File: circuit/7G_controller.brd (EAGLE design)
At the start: 66.3 x 72 mm, 18 parts, among them Q1 3.6864MHz

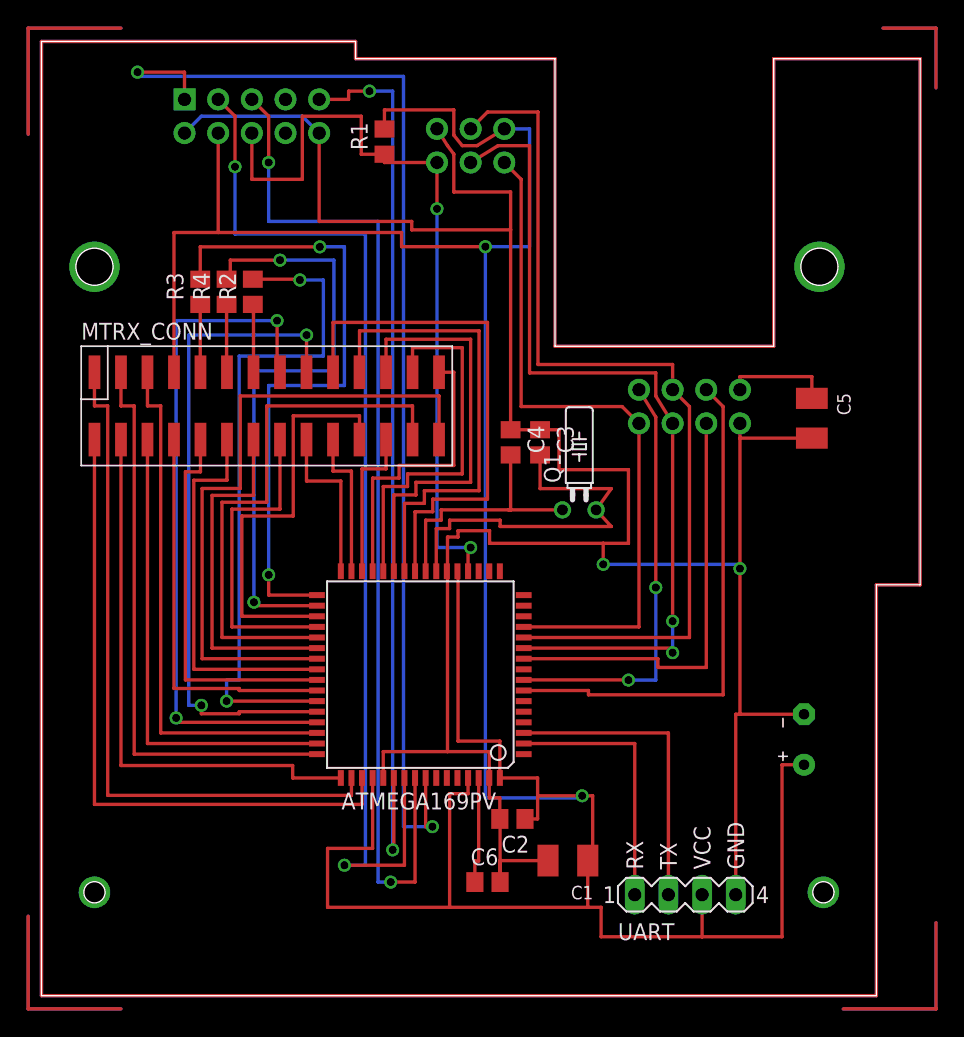
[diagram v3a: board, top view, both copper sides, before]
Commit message: 
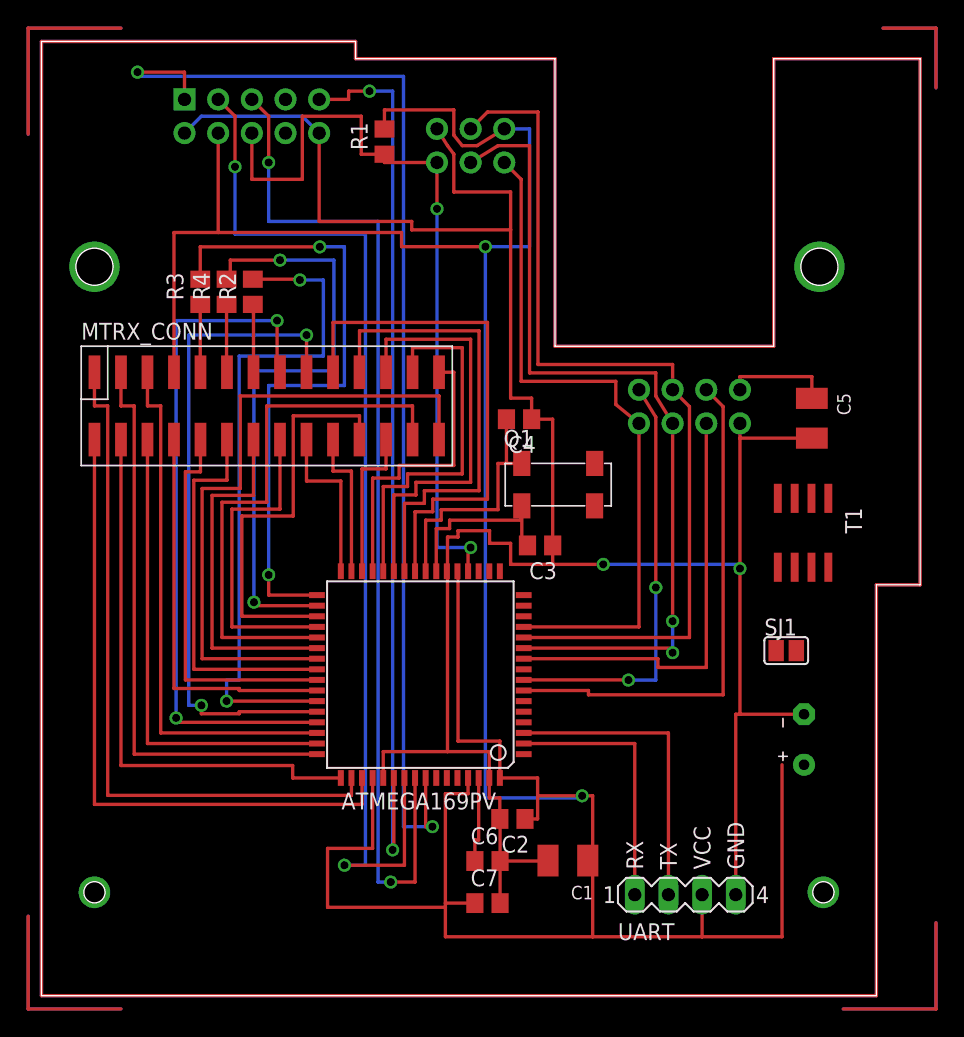
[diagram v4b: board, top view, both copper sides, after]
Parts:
- added C7: 100nF, rcl:C0805
- added SJ1: (no value), jumper:SJ
- added T1: TPS1101D, KileParts:SO8
- C5: value 1uF -> 4.7uF
- NRF24L01: value NRF24L01_MOD_NINE_EAGLES -> NRF24L01_MOD_NINE_EAGLESGENERIC
- Q1: value 3.6864MHz -> 32768Hz; device crystal:TC26H -> KileParts:NSK_QUARTZ_CLOCK
- moved C3 7.78 mm to (37.6, 34.0), turned to 180 degrees
- moved Q1 2.48 mm to (39.0, 38.6)
- moved C4 1.86 mm to (36.0, 43.5), turned to 180 degrees
- moved C6 1.59 mm to (33.7, 10.2)
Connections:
- removed net N$7: ATMEGA169PV.23, C3.2, Q1.2
- new net N$4: BAT1.+, SJ1.2, T1.5, T1.6, T1.7, T1.8
- new net N$6: ATMEGA169PV.23, C3.2, Q1.1
- net GND: now also C7.2, T1.4
- net N$8: now also Q1.4; no longer Q1.1
- net VCC: now also C7.1, SJ1.1, T1.1, T1.2, T1.3; no longer BAT1.+
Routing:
- net N$7: track 29.1 -> 0.00 mm
- net N$6: track 0.00 -> 14.8 mm
- net GND: track 193.4 -> 187.3 mm
- net VCC: track 244.3 -> 247.9 mm
- net AREF: track 8.14 -> 6.55 mm

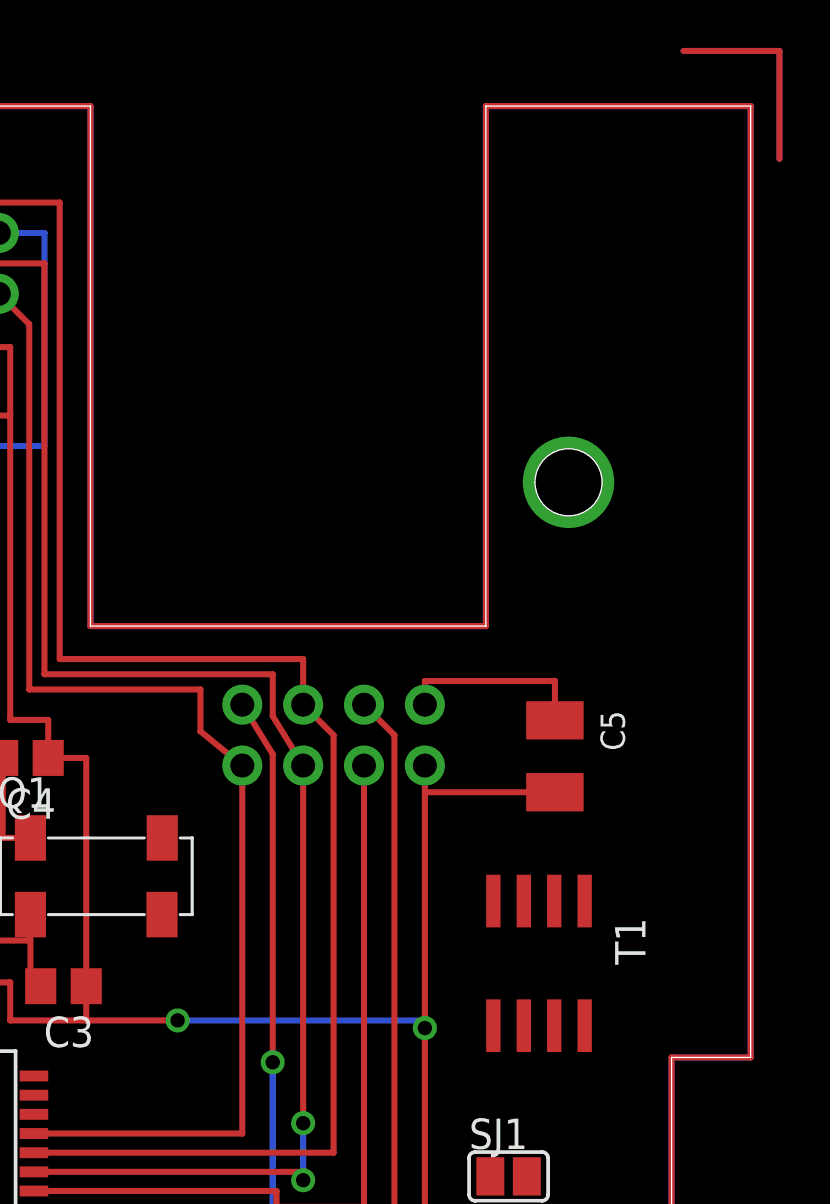
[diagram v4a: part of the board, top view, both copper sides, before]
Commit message: 
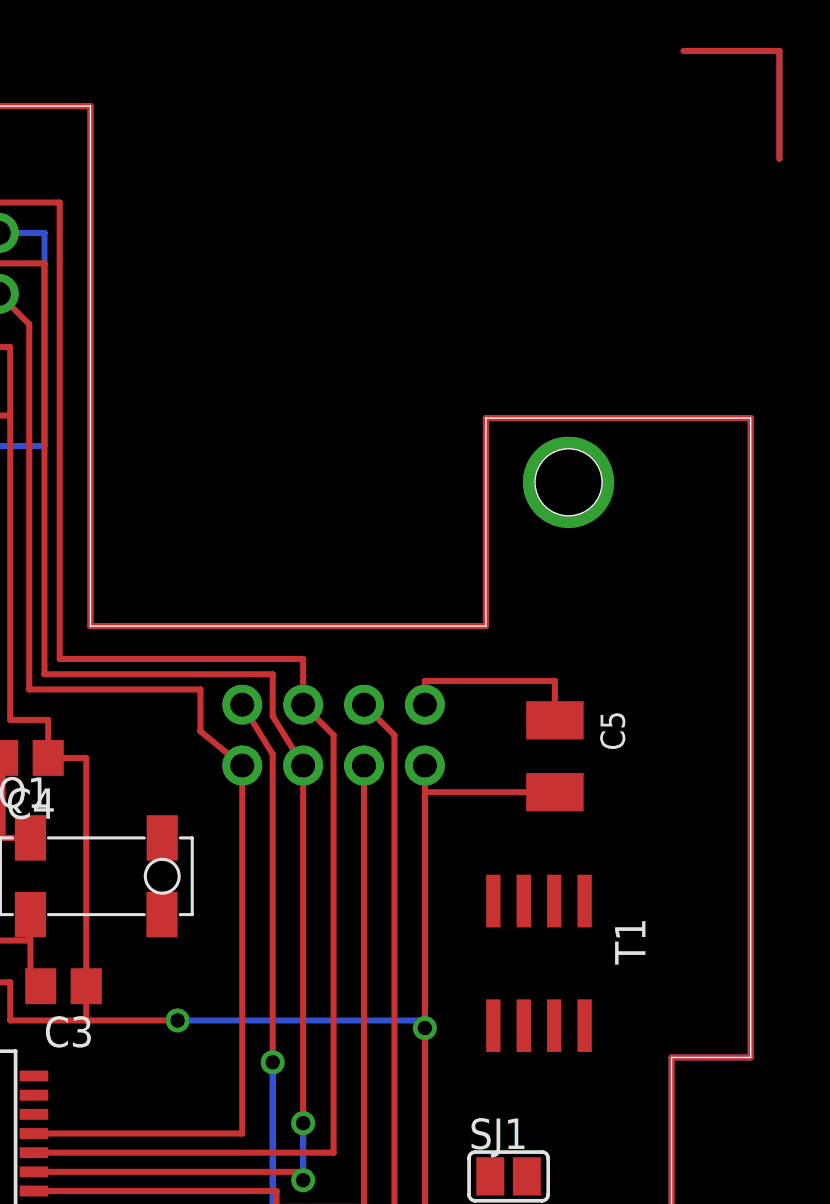
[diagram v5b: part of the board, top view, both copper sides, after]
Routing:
- net N$19: track 320.0 -> 294.0 mm
- net N$1: track 320.0 -> 294.0 mm
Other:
- outline, holes or cut-outs redrawn
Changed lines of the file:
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@@
 <setting verticaltext="up"/>
 </settings>
-<grid distance="0.00625" unitdist="inch" unit="inch" style="lines" multiple="1" display="yes" altdistance="0.025" altunitdist="inch" altunit="inch"/>
+<grid distance="0.0125" unitdist="inch" unit="inch" style="lines" multiple="1" display="yes" altdistance="0.025" altunitdist="inch" altunit="inch"/>
 <layers>
 <layer number="1" name="Top" color="4" fill="1" visible="yes" active="yes"/>
@@
 <wire x1="63" y1="0" x2="63" y2="31" width="0" layer="20"/>
 <wire x1="63" y1="31" x2="66.3" y2="31" width="0" layer="20"/>
-<wire x1="66.3" y1="31" x2="66.3" y2="70.7" width="0" layer="20"/>
-<wire x1="66.3" y1="70.7" x2="55.25" y2="70.7" width="0" layer="20"/>
-<wire x1="55.25" y1="70.7" x2="55.25" y2="49" width="0" layer="20"/>
+<wire x1="66.3" y1="31" x2="66.3" y2="57.6825" width="0" layer="20"/>
+<wire x1="66.3" y1="57.6825" x2="55.25" y2="57.6825" width="0" layer="20"/>
+<wire x1="55.25" y1="57.6825" x2="55.25" y2="49" width="0" layer="20"/>
 <wire x1="55.25" y1="49" x2="38.75" y2="49" width="0" layer="20"/>
 <wire x1="38.75" y1="49" x2="38.75" y2="70.7" width="0" layer="20"/>
@@
 <wire x1="38.75" y1="70.7" x2="38.75" y2="49" width="0.254" layer="16"/>
 <wire x1="38.75" y1="49" x2="55.25" y2="49" width="0.254" layer="16"/>
-<wire x1="55.25" y1="49" x2="55.25" y2="70.7" width="0.254" layer="16"/>
-<wire x1="55.25" y1="70.7" x2="66.3" y2="70.7" width="0.254" layer="16"/>
-<wire x1="66.3" y1="70.7" x2="66.3" y2="31" width="0.254" layer="16"/>
+<wire x1="55.25" y1="49" x2="55.25" y2="57.6825" width="0.254" layer="16"/>
+<wire x1="55.25" y1="57.6825" x2="66.3" y2="57.6825" width="0.254" layer="16"/>
+<wire x1="66.3" y1="57.6825" x2="66.3" y2="31" width="0.254" layer="16"/>
 <wire x1="66.3" y1="31" x2="63" y2="31" width="0.254" layer="16"/>
 <wire x1="63" y1="31" x2="63" y2="0" width="0.254" layer="16"/>
@@
 <wire x1="38.75" y1="70.7" x2="38.75" y2="49" width="0.254" layer="1"/>
 <wire x1="38.75" y1="49" x2="55.25" y2="49" width="0.254" layer="1"/>
-<wire x1="55.25" y1="49" x2="55.25" y2="70.7" width="0.254" layer="1"/>
-<wire x1="55.25" y1="70.7" x2="66.3" y2="70.7" width="0.254" layer="1"/>
-<wire x1="66.3" y1="70.7" x2="66.3" y2="31" width="0.254" layer="1"/>
+<wire x1="55.25" y1="49" x2="55.25" y2="57.6825" width="0.254" layer="1"/>
+<wire x1="55.25" y1="57.6825" x2="66.3" y2="57.6825" width="0.254" layer="1"/>
+<wire x1="66.3" y1="57.6825" x2="66.3" y2="31" width="0.254" layer="1"/>
 <wire x1="66.3" y1="31" x2="63" y2="31" width="0.254" layer="1"/>
 <wire x1="63" y1="31" x2="63" y2="0" width="0.254" layer="1"/>

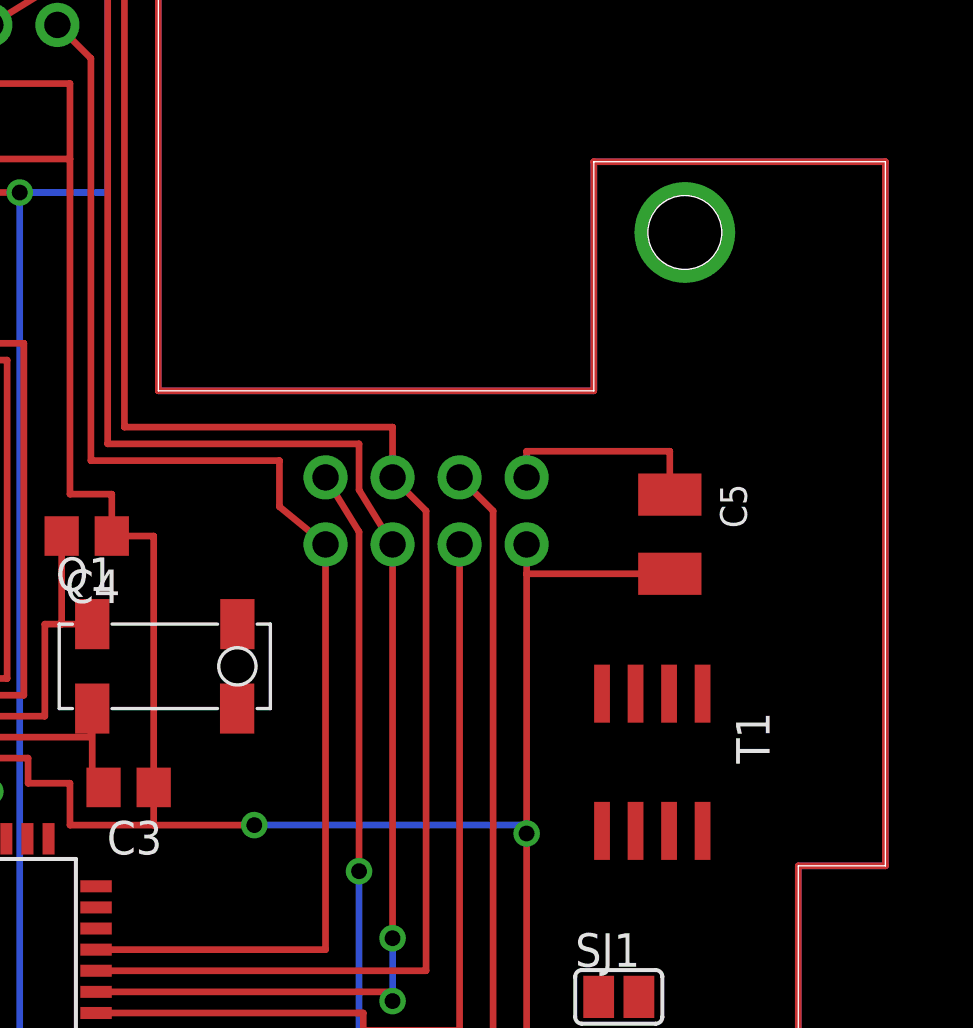
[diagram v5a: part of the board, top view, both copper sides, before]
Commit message: 
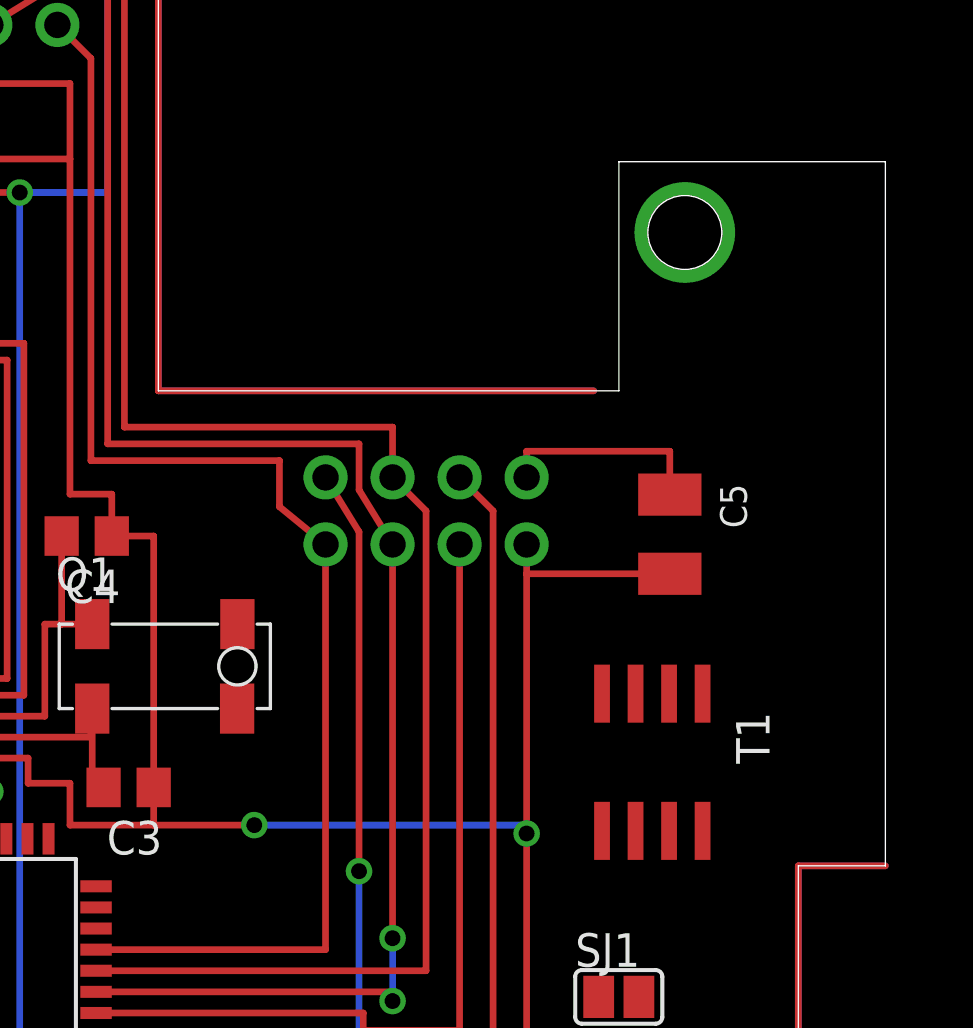
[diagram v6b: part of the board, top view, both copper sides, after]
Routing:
- net N$19: track 294.0 -> 247.6 mm
- net N$1: track 294.0 -> 247.6 mm
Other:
- outline, holes or cut-outs redrawn
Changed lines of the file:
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@@
 <wire x1="63" y1="31" x2="66.3" y2="31" width="0" layer="20"/>
 <wire x1="66.3" y1="31" x2="66.3" y2="57.6825" width="0" layer="20"/>
-<wire x1="66.3" y1="57.6825" x2="55.25" y2="57.6825" width="0" layer="20"/>
-<wire x1="55.25" y1="57.6825" x2="55.25" y2="49" width="0" layer="20"/>
-<wire x1="55.25" y1="49" x2="38.75" y2="49" width="0" layer="20"/>
+<wire x1="66.3" y1="57.6825" x2="56.2025" y2="57.6825" width="0" layer="20"/>
+<wire x1="56.2025" y1="57.6825" x2="56.2025" y2="49" width="0" layer="20"/>
+<wire x1="56.2025" y1="49" x2="38.75" y2="49" width="0" layer="20"/>
 <wire x1="38.75" y1="49" x2="38.75" y2="70.7" width="0" layer="20"/>
 <wire x1="38.75" y1="70.7" x2="23.7" y2="70.7" width="0" layer="20"/>
@@
 <wire x1="38.57375" y1="32.54375" x2="38.57375" y2="33.9725" width="0.254" layer="1"/>
 <wire x1="42.38625" y1="32.54375" x2="38.57375" y2="32.54375" width="0.254" layer="1"/>
-<wire x1="58.13125" y1="42.0675" x2="55.5625" y2="37.525" width="0" layer="19" extent="1-1"/>
 <wire x1="35.40125" y1="57.785" x2="35.40125" y2="45.085" width="0.254" layer="1"/>
 <wire x1="35.40125" y1="45.085" x2="36.98625" y2="45.085" width="0.254" layer="1"/>
 <wire x1="36.98625" y1="45.085" x2="36.98625" y2="43.4975" width="0.254" layer="1"/>
+<wire x1="58.13125" y1="42.0675" x2="55.5625" y2="37.525" width="0" layer="19" extent="1-1"/>
 </signal>
 <signal name="MOSI">
@@
 <wire x1="38.75" y1="70.7" x2="38.75" y2="49" width="0.254" layer="16"/>
 <wire x1="38.75" y1="49" x2="55.25" y2="49" width="0.254" layer="16"/>
-<wire x1="55.25" y1="49" x2="55.25" y2="57.6825" width="0.254" layer="16"/>
-<wire x1="55.25" y1="57.6825" x2="66.3" y2="57.6825" width="0.254" layer="16"/>
-<wire x1="66.3" y1="57.6825" x2="66.3" y2="31" width="0.254" layer="16"/>
 <wire x1="66.3" y1="31" x2="63" y2="31" width="0.254" layer="16"/>
 <wire x1="63" y1="31" x2="63" y2="0" width="0.254" layer="16"/>
@@
 <wire x1="38.75" y1="70.7" x2="38.75" y2="49" width="0.254" layer="1"/>
 <wire x1="38.75" y1="49" x2="55.25" y2="49" width="0.254" layer="1"/>
-<wire x1="55.25" y1="49" x2="55.25" y2="57.6825" width="0.254" layer="1"/>
-<wire x1="55.25" y1="57.6825" x2="66.3" y2="57.6825" width="0.254" layer="1"/>
-<wire x1="66.3" y1="57.6825" x2="66.3" y2="31" width="0.254" layer="1"/>
 <wire x1="66.3" y1="31" x2="63" y2="31" width="0.254" layer="1"/>
 <wire x1="63" y1="31" x2="63" y2="0" width="0.254" layer="1"/>
